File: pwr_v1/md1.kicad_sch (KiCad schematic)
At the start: 17 parts, among them M1 Conn_01x08_Socket

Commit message: Schematic and layout updated
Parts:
- 1C1: footprint Capacitor_SMD:C_0805_2012Metric -> Capacitor_SMD:C_0402_1005Metric
- 1C2, 1C4, 1C6: footprint Capacitor_SMD:C_0603_1608Metric -> Capacitor_SMD:C_0402_1005Metric
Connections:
- net GNDREF renamed GND
- net GND: no longer 1C6.2, 1U1.4 (GND_BK), M1.4 (Pin_4)
- new net GND_BK: 1C6.2, 1U1.4 (GND_BK), M1.4 (Pin_4)

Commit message: Schematic updated
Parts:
- 1R1: footprint Resistor_SMD:R_0603_1608Metric_Pad0.98x0.95mm_HandSolder -> Resistor_SMD:R_0603_1608Metric
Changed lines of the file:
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@@
+	)
+	(symbol
+		(lib_id "Device:R_Small_US")
+		(at 115.824 54.61 0)
+		(unit 1)
+		(exclude_from_sim no)
+		(in_bom yes)
+		(on_board yes)
+		(dnp no)
+		(property "Reference" "1R1"
+			(at 117.094 53.848 0)
+			(effects
+				(font
+					(size 1.27 1.27)
+				)
+				(justify left)
+			)
+		)
+		(property "Value" "5k1"
+			(at 117.094 55.626 0)
+			(effects
+				(font
+					(size 1.27 1.27)
+				)
+				(justify left)
+			)
+		)
+		(property "Footprint" "Resistor_SMD:R_0603_1608Metric"
+			(at 115.824 54.61 0)
+			(effects
+				(font
+					(size 1.27 1.27)
+				)
+				(hide yes)
+			)
+		)
+		(property "Datasheet" "~"
+			(at 115.824 54.61 0)
+			(effects
+				(font
+					(size 1.27 1.27)
+				)
+				(hide yes)
+			)
+		)
+		(property "Description" "MFR.Part # ERJ3GEYJ512V JLCPCB Part # C403509"
+			(at 115.824 54.61 0)
+			(effects
+				(font
+					(size 1.27 1.27)
+				)
+				(hide yes)
+			)
+		)
+		(pin "1"
+		)
+		(pin "2"
+		)
+		(instances
+			(project "pwr_v1"
+				(path "/42eee4f9-ea65-4e89-8296-df9554a24009/f5214ba6-8304-44b3-b1c8-230e23716682"
+					(reference "1R1")
+					(unit 1)
+				)
+			)
+		)
 	)
 	(symbol
@@
 	)
 	(symbol
-		(lib_id "Device:R_Small_US")
-		(at 115.824 54.61 0)
-		(unit 1)
-		(exclude_from_sim no)
-		(in_bom yes)
-		(on_board yes)
-		(dnp no)
-		(property "Reference" "1R1"
-			(at 110.744 53.34 0)
-			(effects
-				(font
-					(size 1.27 1.27)
-				)
-				(justify left)
-			)
-		)
-		(property "Value" "5k1"
-			(at 110.744 55.118 0)
-			(effects
-				(font
-					(size 1.27 1.27)
-				)
-				(justify left)
-			)
-		)
-		(property "Footprint" "Resistor_SMD:R_0603_1608Metric_Pad0.98x0.95mm_HandSolder"
-			(at 115.824 54.61 0)
-			(effects
-				(font
-					(size 1.27 1.27)
-				)
-				(hide yes)
-			)
-		)
-		(property "Datasheet" "~"
-			(at 115.824 54.61 0)
-			(effects
-				(font
-					(size 1.27 1.27)
-				)
-				(hide yes)
-			)
-		)
-		(property "Description" "Resistor, small US symbol"
-			(at 115.824 54.61 0)
-			(effects
-				(font
-					(size 1.27 1.27)
-				)
-				(hide yes)
-			)
-		)
-		(pin "1"
-		)
-		(pin "2"
-		)
-		(instances
-			(project "pwr_v1"
-				(path "/42eee4f9-ea65-4e89-8296-df9554a24009/f5214ba6-8304-44b3-b1c8-230e23716682"
-					(reference "1R1")
-					(unit 1)
-				)
-			)
-		)
-	)
-	(symbol
 		(lib_id "Device:C")
 		(at 184.404 55.88 0)
@@
 			)
 		)
-		(property "Description" "Resistor, small US symbol"
+		(property "Description" "MFR.Part # ERJ3GEYJ512V JLCPCB Part # C403509"
 			(at 122.174 54.61 0)
 			(effects

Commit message: Sch and Layout updated; Added batt sup ckt, placed and routed all motor drivers.
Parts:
- M1: footprint Connector_PinHeader_2.54mm:PinHeader_1x08_P2.54mm_Vertical_SMD_Pin1Left -> Connector_PinHeader_2.54mm:PinHeader_1x08_P2.54mm_Vertical
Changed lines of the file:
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@@
 			)
 		)
-		(property "Footprint" "Connector_PinHeader_2.54mm:PinHeader_1x08_P2.54mm_Vertical_SMD_Pin1Left"
+		(property "Footprint" "Connector_PinHeader_2.54mm:PinHeader_1x08_P2.54mm_Vertical"
 			(at 245.364 106.68 0)
 			(effects

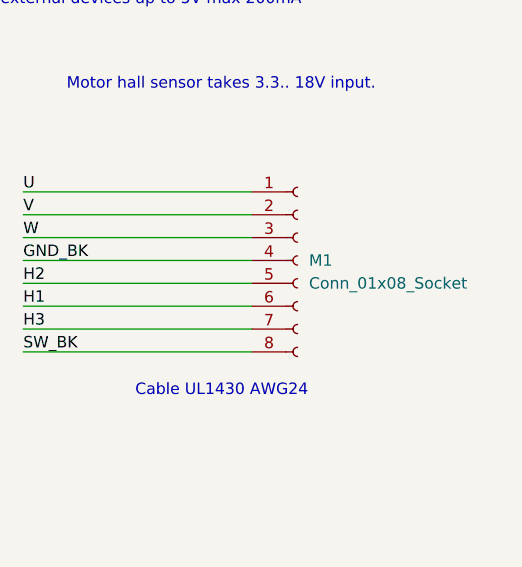
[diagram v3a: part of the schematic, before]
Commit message: Schematic and layout updated; Motor driver alignments and planes;  Few components updated
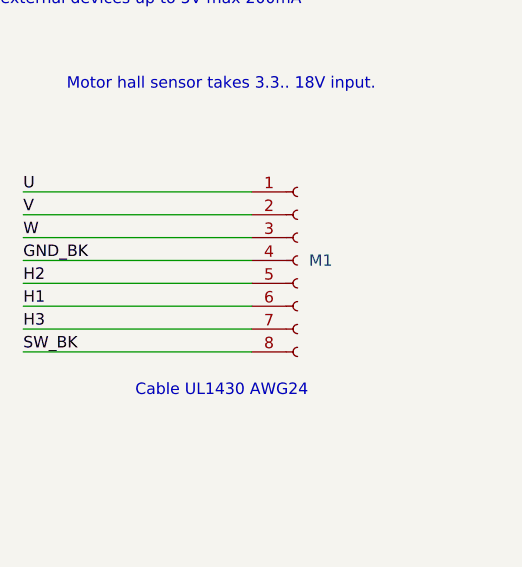
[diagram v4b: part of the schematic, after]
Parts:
- M1: footprint Connector_PinHeader_2.54mm:PinHeader_1x08_P2.54mm_Vertical -> Connector_Molex:Molex_KK-254_AE-6410-08A_1x08_P2.54mm_Vertical
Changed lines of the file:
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@@
 				)
 				(justify left)
+				(hide yes)
 			)
 		)
-		(property "Footprint" "Connector_PinHeader_2.54mm:PinHeader_1x08_P2.54mm_Vertical"
+		(property "Footprint" "Connector_Molex:Molex_KK-254_AE-6410-08A_1x08_P2.54mm_Vertical"
 			(at 245.364 106.68 0)
 			(effects
@@
 			)
 		)
-		(property "Description" "MFR.Part # X6511WVS-08H-C60D48R2 JLCPCB Part # C2883765"
+		(property "Description" ""
 			(at 245.364 106.68 0)
 			(effects

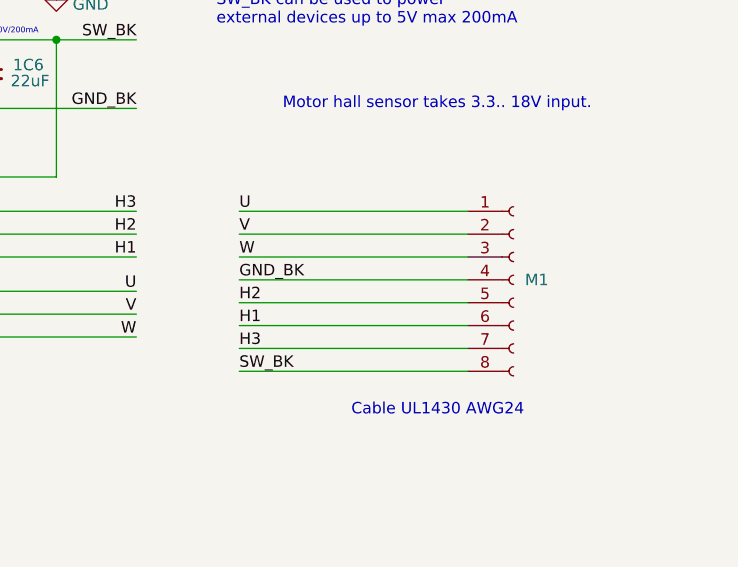
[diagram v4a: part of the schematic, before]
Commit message: Schematic and layout updated; Layout placement and routing completed
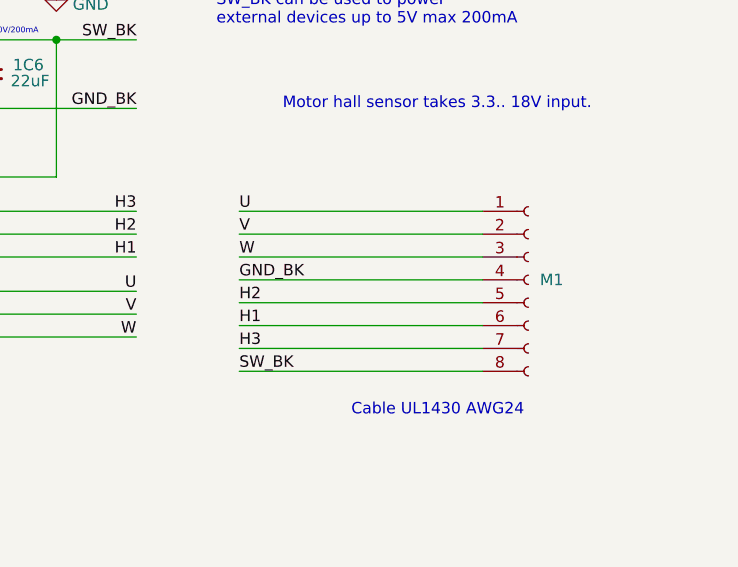
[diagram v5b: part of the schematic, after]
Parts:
- M1: footprint Connector_Molex:Molex_KK-254_AE-6410-08A_1x08_P2.54mm_Vertical -> Connector_PinHeader_2.54mm:PinHeader_1x08_P2.54mm_Vertical

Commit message: Sch: 0ohm res added to SPI pins, MD footprints updated; Lay: Silkscreen aligned, logo added, DRC
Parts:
- 1U1: footprint MTR:RGF0040E-IPC_B -> motorDriver:RGF0040E-IPC_B
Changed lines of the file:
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@@
 			)
 		)
-		(property "Footprint" "MTR:RGF0040E-IPC_B"
+		(property "Footprint" "motorDriver:RGF0040E-IPC_B"
 			(at 217.424 57.15 0)
 			(effects

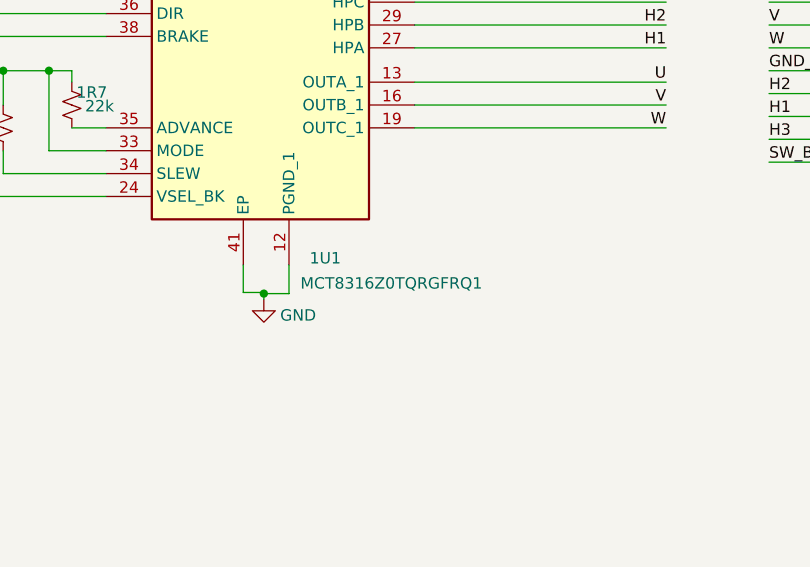
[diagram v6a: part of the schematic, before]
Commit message: Sch: DNP updated, JLC part numbers updated for all components; Lay: Fiducial placement, routing aligned.
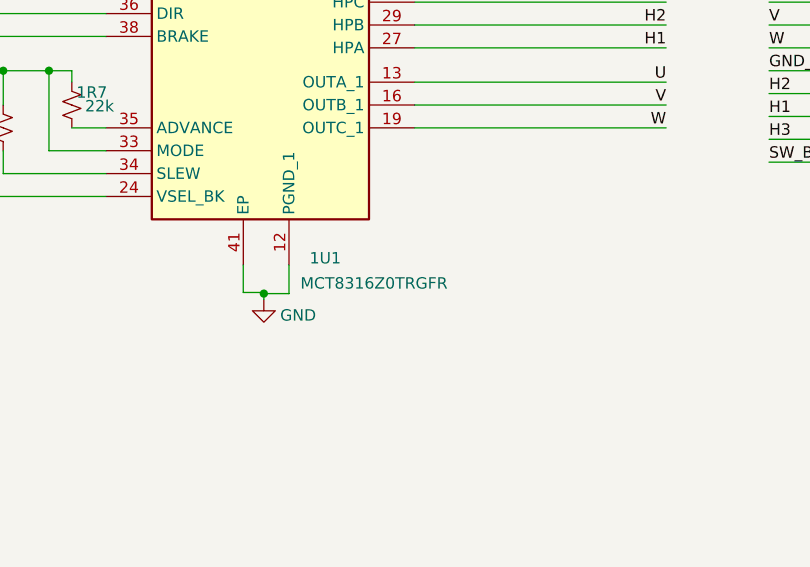
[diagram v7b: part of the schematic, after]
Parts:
- 1U1: value MCT8316Z0TQRGFRQ1 -> MCT8316Z0TRGFR
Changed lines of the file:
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@@
 			)
 		)
-		(property "Description" "Resistor, small US symbol"
+		(property "Description" "MFR.Part # 0402WGF4702TCE JLCPCB Part # C25792"
 			(at 129.794 113.03 0)
 			(effects
@@
 			)
 		)
-		(property "Value" "MCT8316Z0TQRGFRQ1"
+		(property "Value" "MCT8316Z0TRGFR"
 			(at 162.814 130.302 0)
 			(effects
@@
 			)
 		)
-		(property "Description" ""
+		(property "Description" "MFR.Part # MCT8316Z0TRGFR JLCPCB Part # C3681342"
 			(at 141.224 69.85 0)
 			(effects
@@
 			)
 		)
-		(property "Description" "Resistor, small US symbol"
+		(property "Description" "MFR.Part # 0603WAF2002T5E JLCPCB Part # C4184"
 			(at 128.905 68.58 0)
 			(effects
@@
 			)
 		)
-		(property "Description" "Resistor, small US symbol"
+		(property "Description" "MFR.Part # 0402WGJ0223TCE JLCPCB Part # C25547"
 			(at 137.414 110.49 0)
 			(effects
@@
 			)
 		)
-		(property "Description" ""
+		(property "Description" "MFR.Part # HB-PH3-25418PB2GOP JLCPCB Part # C6332201"
 			(at 247.015 106.68 0)
 			(effects
@@
 			)
 		)
-		(property "Description" "Resistor, small US symbol"
+		(property "Description" "MFR.Part # 0603WAF2702T5E JLCPCB Part # C22967"
 			(at 128.905 54.61 0)
 			(effects
@@
 			)
 		)
-		(property "Description" "Resistor, small US symbol"
+		(property "Description" "MFR.Part # RC0805FR-071ML JLCPCB Part # C107700"
 			(at 123.444 113.03 0)
 			(effects

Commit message: Final PCB files sent for fab
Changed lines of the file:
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@@
+	(wire
+		(pts
+			(xy 184.404 59.69) (xy 204.47 59.69)
+		)
+		(stroke
+			(width 0)
+			(type default)
+		)
+	)
 	(wire
 		(pts
@@
 		(pts
 			(xy 129.794 106.68) (xy 134.874 106.68)
-		)
-		(stroke
-			(width 0)
-			(type default)
-		)
-	)
-	(wire
-		(pts
-			(xy 184.404 59.69) (xy 204.724 59.69)
 		)
 		(stroke
@@
 		)
 	)
-	(label "VM"
-		(at 171.704 50.8 180)
-		(fields_autoplaced yes)
-		(effects
-			(font
-				(size 1.27 1.27)
-			)
-			(justify right bottom)
-		)
-	)
-	(hierarchical_label "GND"
-		(shape input)
-		(at 204.724 59.69 0)
-		(fields_autoplaced yes)
-		(effects
-			(font
-				(size 1.27 1.27)
-			)
-			(justify left)
-		)
-	)
 	(hierarchical_label "FGOUT"
 		(shape input)
@@
 		)
 	)
+	(hierarchical_label "GND"
+		(shape input)
+		(at 204.47 59.69 0)
+		(fields_autoplaced yes)
+		(effects
+			(font
+				(size 1.27 1.27)
+			)
+			(justify left)
+		)
+	)
